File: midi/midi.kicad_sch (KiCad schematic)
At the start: 42 parts, among them CON1 SJ1-3523N, M1 Si4412DY, U1 ESP32-S3-WROOM-1-n16, U2 LTC1624CS8_TRPBF, U3 MAX98357A, U4 MAX98357A

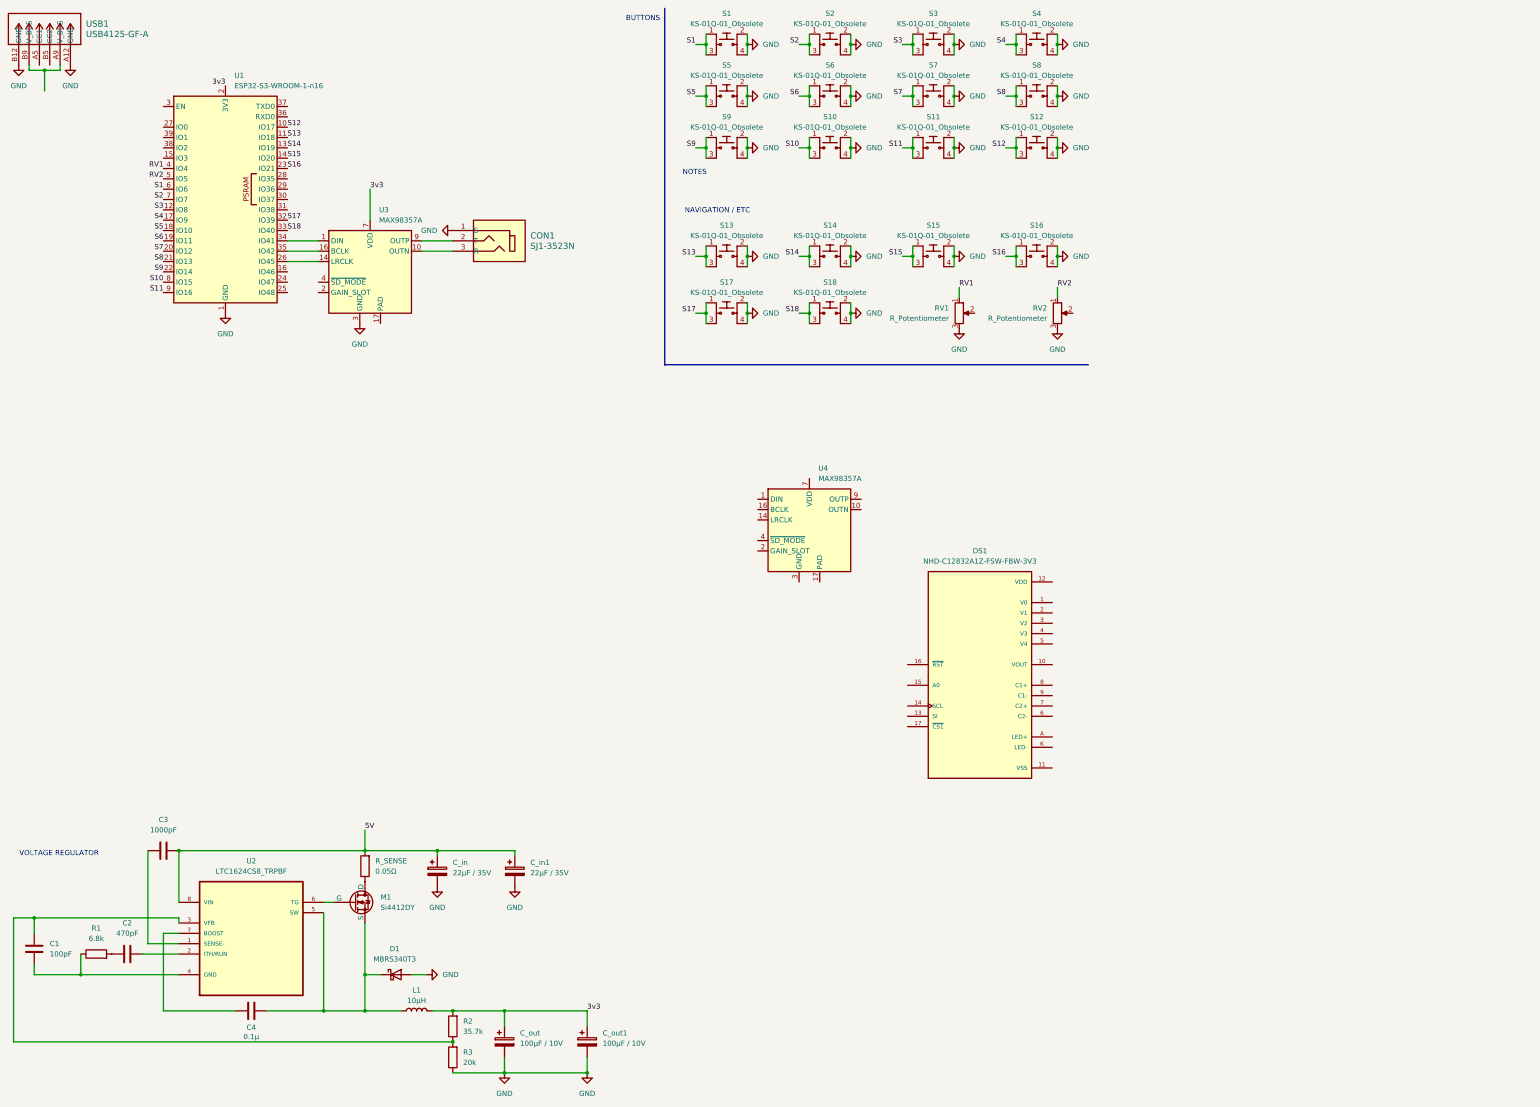
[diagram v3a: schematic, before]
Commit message: schematic: link up audio i2s & LCD SPI bus
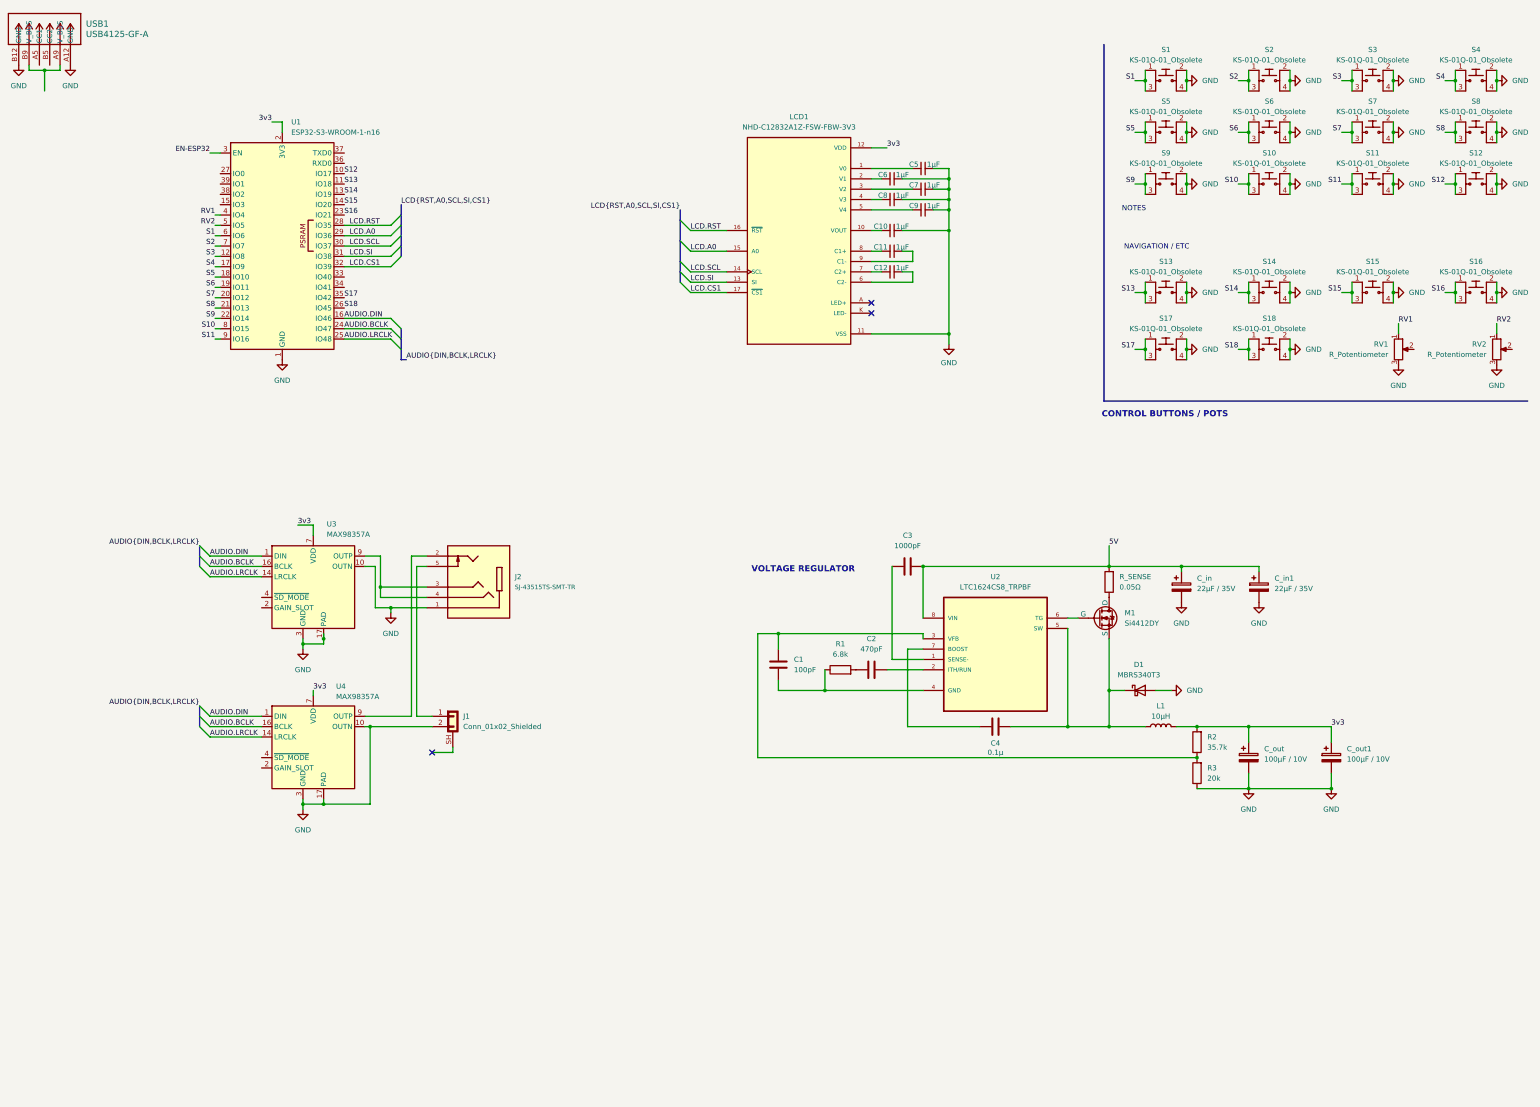
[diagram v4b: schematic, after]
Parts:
- removed CON1: SJ1-3523N, digikey-footprints:Headphone_Jack_3.5mm_SJ1-3523N, symbol dk_Barrel-Audio-Connectors:SJ1-3523N
- added C10, C11, C12, C5, C6, C7, C8, C9: 1µF, symbol Device:C_Small
- added J1: Conn_01x02_Shielded, symbol Connector_Generic_Shielded:Conn_01x02_Shielded
- added J2: SJ-43515TS-SMT-TR, SJ-43515TS-SMT-TR:CUI_SJ-43515TS-SMT-TR, symbol SJ-43515TS-SMT-TR:SJ-43515TS-SMT-TR
- renumbered DS1 to LCD1
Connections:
- net 3v3: now also LCD1.12 (VDD), U4.7 (VDD), U4.8 (VDD)
- net GND: now also LCD1.11 (VSS), U3.10 (OUTN), U3.17 (PAD), U4.10 (OUTN), U4.11 (GND), U4.15 (GND), U4.17 (PAD), U4.3 (GND), C10.1, C5.1, C6.1, C7.1, C8.1, C9.1, J1.2 (Pin_2), J2.1
- net S17: now also U1.35 (IO42); no longer U1.32 (IO39)
- net S18: now also U1.26 (IO45); no longer U1.33 (IO40)
- net at U1.34 (IO41): no longer U3.1 (DIN)
- net AUDIO.LRCLK: now reaches U3.14 (LRCLK)
- net AUDIO.LRCLK: now also U1.25 (IO48), U4.14 (LRCLK); no longer U1.26 (IO45)
- net AUDIO.BCLK: now reaches U3.16 (BCLK)
- net AUDIO.BCLK: now also U1.24 (IO47), U4.16 (BCLK); no longer U1.35 (IO42)
- net at U3.9 (OUTP): now also J2.3, J2.4
- net at LCD1.1 (V0): now also C5.2
- net at LCD1.10 (VOUT): now also C10.2
- net LCD.SI: now reaches LCD1.13 (SI)
- net LCD.SI: now also U1.31 (IO38)
- net LCD.SCL: now reaches LCD1.14 (SCL)
- net LCD.SCL: now also U1.30 (IO37)
- net LCD.A0: now reaches LCD1.15 (A0)
- net LCD.A0: now also U1.29 (IO36)
- net LCD.RST: now reaches LCD1.16 (~{RST})
- net LCD.RST: now also U1.28 (IO35)
- net LCD.CS1: now reaches LCD1.17 (~{CS1})
- net LCD.CS1: now also U1.32 (IO39)
- net at LCD1.2 (V1): now also C6.2
- net at LCD1.3 (V2): now also C7.2
- net at LCD1.4 (V3): now also C8.2
- net at LCD1.5 (V4): now also C9.2
- net at LCD1.6 (C2-): now also C12.1
- net at LCD1.7 (C2+): now also C12.2
- net at LCD1.8 (C1+): now also C11.2
- net at LCD1.9 (C1-): now also C11.1
- net AUDIO.DIN: now reaches U1.16 (IO46)
- net AUDIO.DIN: now also U3.1 (DIN), U4.1 (DIN)
- net EN-ESP32: now reaches U1.3 (EN)
- net at U4.9 (OUTP): now also J2.2
- new net: J1.1 (Pin_1), J2.5
- no-connect marks 0 -> 3
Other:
- note added: "CONTROL BUTTONS / POTS"
- note removed: "BUTTONS"
- moved on the sheet: C1, C2, C3, C4, C_in, C_in1, C_out, C_out1, D1, L1, LCD1, M1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

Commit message: add button input mux
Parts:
- removed S17, S18: KS-01Q-01_Obsolete, digikey-footprints:PushButton_Round_D12mm_THT_KS-01Q-01, symbol dk_Pushbutton-Switches:KS-01Q-01_Obsolete
- added U5: CD74HC154M96, DW24, symbol MUX_CD74HC154M96:CD74HC154M96
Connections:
- net 5V: now also USB1.A9 (V_BUS), USB1.B9 (V_BUS)
- net GND: now also U5.12 (GND)
- net S1: now also U5.1 (*Y0); no longer U1.6 (IO6)
- net S10: now also U5.10 (*Y9); no longer U1.8 (IO15)
- net S11: now also U5.11 (*Y10); no longer U1.9 (IO16)
- net S12: now also U5.13 (*Y11); no longer U1.10 (IO17)
- net S13: now also U5.14 (*Y12); no longer U1.11 (IO18)
- net S14: now also U5.15 (*Y13); no longer U1.13 (IO19)
- net S15: now also U5.16 (*Y14); no longer U1.14 (IO20)
- net S16: now also U5.17 (*Y15); no longer U1.23 (IO21)
- net S2: now also U5.2 (*Y1); no longer U1.7 (IO7)
- net S3: now also U5.3 (*Y2); no longer U1.12 (IO8)
- net S4: now also U5.4 (*Y3); no longer U1.17 (IO9)
- net S5: now also U5.5 (*Y4); no longer U1.18 (IO10)
- net S6: now also U5.6 (*Y5); no longer U1.19 (IO11)
- net S7: now also U5.7 (*Y6); no longer U1.20 (IO12)
- net S8: now also U5.8 (*Y7); no longer U1.21 (IO13)
- net S9: now also U5.9 (*Y8); no longer U1.22 (IO14)
- net 3v3 renamed 3V3
- net 3V3: now also U5.24 (VCC)
- new net BTND0: U1.17 (IO9), U5.23 (A0)
- new net BTND1: U1.12 (IO8), U5.22 (A1)
- new net BTND2: U1.7 (IO7), U5.21 (A2)
- new net BTND3: U1.6 (IO6), U5.20 (A3)
- no-connect marks 3 -> 4
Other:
- note added: "AUDIO OUTPUT"
- note added: "CONTROL BUTTONS BUTTON INPUT MUX POTS"
- note added: "ESP32 MCU"
- note added: "LCD DISPLAY"
- note added: "USB CONNECTOR"
- note removed: "CONTROL BUTTONS / POTS"
- moved on the sheet: C1, C10, C11, C12, C2, C3, C4, C5, C6, C7, C8, C9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

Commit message: updates
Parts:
- renumbered C_in to C_in2, C_out to C_out2, R_SENSE to R_SENSE1
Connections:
- net 3V3: now also RV1.1, RV2.1
- net GND: no longer J1.2 (Pin_2), U4.10 (OUTN)
- net RV1: now also RV1.2; no longer RV1.1
- net RV2: now also RV2.2; no longer RV2.1
- new net: J1.2 (Pin_2), U4.10 (OUTN)
- no-connect marks 4 -> 25

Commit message: added footprints for caps and some others
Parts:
- C1, C4: footprint (none) -> Capacitor_SMD:C_1210_3225Metric
- C10, C11, C12, C5, C6, C7, C8, C9: footprint (none) -> Capacitor_SMD:C_0603_1608Metric
- C2: footprint (none) -> Capacitor_SMD:C_1812_4532Metric
- C3: footprint (none) -> Capacitor_SMD:C_0805_2012Metric
- C_in1, C_in2: footprint (none) -> Capacitor_SMD:C_2220_5750Metric
- C_out1, C_out2: footprint (none) -> Capacitor_THT:CP_Radial_D6.3mm_P2.50mm
- D1: footprint (none) -> Diode_SMD:D_SMA
- J1: footprint (none) -> Connector_PinHeader_2.54mm:PinHeader_1x02_P2.54mm_Horizontal
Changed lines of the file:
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@@
 			)
 		)
-		(property "Footprint" ""
+		(property "Footprint" "Capacitor_SMD:C_1812_4532Metric"
 			(at 194.31 148.8948 0)
 			(effects
@@
 			)
 		)
-		(property "Footprint" ""
+		(property "Footprint" "Capacitor_SMD:C_0603_1608Metric"
 			(at 205.74 49.53 0)
 			(effects
@@
 			)
 		)
-		(property "Footprint" ""
+		(property "Footprint" "Capacitor_SMD:C_0805_2012Metric"
 			(at 203.2 123.4948 0)
 			(effects
@@
 			)
 		)
-		(property "Footprint" ""
+		(property "Footprint" "Capacitor_SMD:C_0603_1608Metric"
 			(at 205.74 67.31 0)
 			(effects
@@
 			)
 		)
-		(property "Footprint" ""
+		(property "Footprint" "Capacitor_SMD:C_0603_1608Metric"
 			(at 205.74 62.23 0)
 			(effects
@@
 			)
 		)
-		(property "Footprint" ""
+		(property "Footprint" "Capacitor_SMD:C_0603_1608Metric"
 			(at 205.74 44.45 0)
 			(effects
@@
 			)
 		)
-		(property "Footprint" ""
+		(property "Footprint" "Capacitor_SMD:C_2220_5750Metric"
 			(at 286.7152 133.35 0)
 			(effects
@@
 			)
 		)
-		(property "Footprint" ""
+		(property "Footprint" "Connector_PinHeader_2.54mm:PinHeader_1x02_P2.54mm_Horizontal"
 			(at 107.95 163.83 0)
 			(effects
@@
 			)
 		)
-		(property "Footprint" ""
+		(property "Footprint" "Diode_SMD:D_SMA"
 			(at 256.54 154.94 0)
 			(effects
@@
 			)
 		)
-		(property "Footprint" ""
+		(property "Footprint" "Capacitor_THT:CP_Radial_D6.3mm_P2.50mm"
 			(at 284.1752 175.26 0)
 			(effects
@@
 			)
 		)
-		(property "Footprint" ""
+		(property "Footprint" "Capacitor_SMD:C_1210_3225Metric"
 			(at 224.79 162.8648 0)
 			(effects
@@
 			)
 		)
-		(property "Footprint" ""
+		(property "Footprint" "Capacitor_SMD:C_0603_1608Metric"
 			(at 213.36 41.91 0)
 			(effects
@@
 			)
 		)
-		(property "Footprint" ""
+		(property "Footprint" "Capacitor_SMD:C_1210_3225Metric"
 			(at 168.6052 152.4 0)
 			(effects
@@
 			)
 		)
-		(property "Footprint" ""
+		(property "Footprint" "Capacitor_SMD:C_2220_5750Metric"
 			(at 267.6652 133.35 0)
 			(effects
@@
 			)
 		)
-		(property "Footprint" ""
+		(property "Footprint" "Capacitor_SMD:C_0603_1608Metric"
 			(at 205.74 57.15 0)
 			(effects
@@
 			)
 		)
-		(property "Footprint" ""
+		(property "Footprint" "Capacitor_SMD:C_0603_1608Metric"
 			(at 213.36 52.07 0)
 			(effects
@@
 			)
 		)
-		(property "Footprint" ""
+		(property "Footprint" "Capacitor_SMD:C_0603_1608Metric"
 			(at 213.36 46.99 0)
 			(effects
@@
 			)
 		)
-		(property "Footprint" ""
+		(property "Footprint" "Capacitor_THT:CP_Radial_D6.3mm_P2.50mm"
 			(at 304.4952 175.26 0)
 			(effects

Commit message: downloaded L1 footprint
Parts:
- U5: footprint DW24 -> MUX_CD74HC154M96:DW24
- USB1: footprint CONN6_USB4125_GCT -> USB4125_GF_A:CONN6_USB4125_GCT
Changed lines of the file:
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@@
 			)
 		)
-		(property "Footprint" "DW24"
+		(property "Footprint" "MUX_CD74HC154M96:DW24"
 			(at 271.78 62.23 0)
 			(effects
@@
 			)
 		)
-		(property "Footprint" "CONN6_USB4125_GCT"
+		(property "Footprint" "USB4125_GF_A:CONN6_USB4125_GCT"
 			(at 352.806 144.526 0)
 			(effects
